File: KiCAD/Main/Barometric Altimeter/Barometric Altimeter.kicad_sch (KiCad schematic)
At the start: 7 parts, among them U11 BMP390L, U12 BMP390L, U13 BMP390L

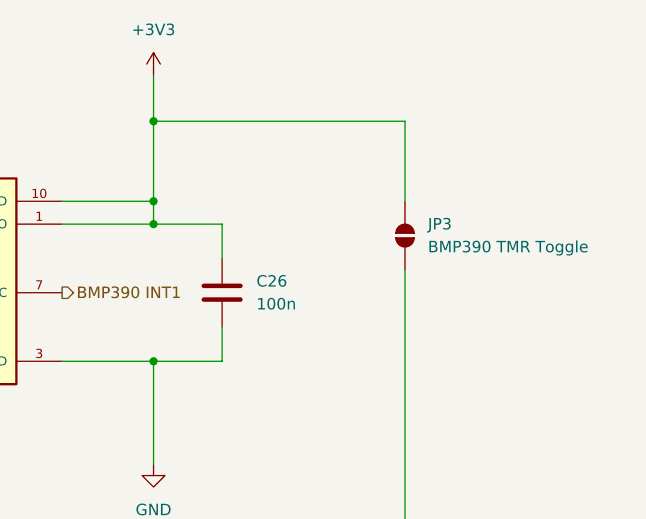
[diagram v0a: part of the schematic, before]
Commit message: Moved custom footprints into local KiCAD footprint library
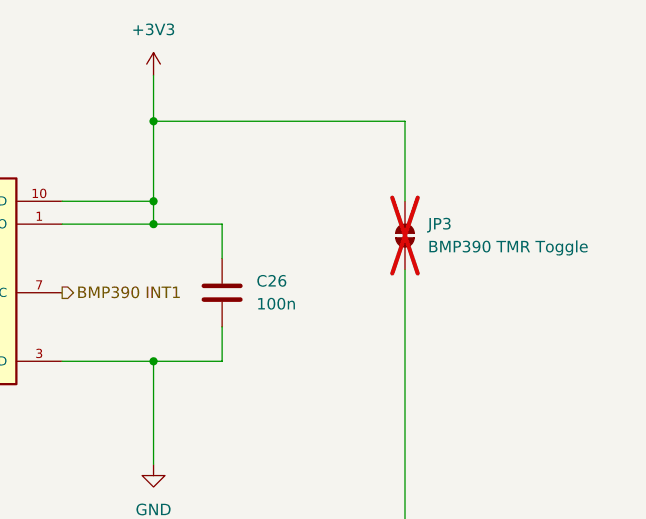
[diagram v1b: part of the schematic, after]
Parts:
- JP3: footprint Resistor_SMD:R_0603_1608Metric_Pad0.98x0.95mm_HandSolder -> Jumper:SolderJumper-2_P1.3mm_Open_TrianglePad1.0x1.5mm; now not fitted
- U11, U12, U13: footprint BMP390L:XDCR_BMP390L -> LRI:XDCR_BMP390L
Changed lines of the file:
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@@
 		(in_bom no)
 		(on_board yes)
-		(dnp no)
+		(dnp yes)
 		(fields_autoplaced yes)
 		(property "Reference" "JP3"
@@
 			)
 		)
-		(property "Footprint" "Resistor_SMD:R_0603_1608Metric_Pad0.98x0.95mm_HandSolder"
+		(property "Footprint" "Jumper:SolderJumper-2_P1.3mm_Open_TrianglePad1.0x1.5mm"
 			(at 162.56 43.18 0)
 			(effects
@@
 			)
 		)
-		(property "Footprint" "BMP390L:XDCR_BMP390L"
+		(property "Footprint" "LRI:XDCR_BMP390L"
 			(at 104.14 107.95 0)
 			(effects
@@
 			)
 		)
-		(property "Footprint" "BMP390L:XDCR_BMP390L"
+		(property "Footprint" "LRI:XDCR_BMP390L"
 			(at 104.14 49.53 0)
 			(effects
@@
 			)
 		)
-		(property "Footprint" "BMP390L:XDCR_BMP390L"
+		(property "Footprint" "LRI:XDCR_BMP390L"
 			(at 104.14 166.37 0)
 			(effects
